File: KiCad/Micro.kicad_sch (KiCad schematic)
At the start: 0 parts

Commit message: Afegit el micro i les etapes del bus CAN i USART, també afegit el cristall i el debug
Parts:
- added C1, C2, C5, C6, C7, C8, C9: 100nF, symbol Device:C
- added C3, C4: 15pF, symbol Device:C
- added J1, J2: DE9_Pins, symbol Connector:DE9_Pins
- added J3: Conn_01x05, symbol Connector_Generic:Conn_01x05
- added R1: 120, symbol Device:R_US
- added U1: PIC24HJ128GP502, Package_SO:SOIC-28W_7.5x17.9mm_P1.27mm, symbol A_David_Puges_sym:PIC24HJ128GP502
- added U2: MCP2562-E-SN, Package_SO:SOIC-8_3.9x4.9mm_P1.27mm, symbol Interface_CAN_LIN:MCP2562-E-SN
- added U3: MAX3232, symbol Interface_UART:MAX3232
- added Y1: Crystal, Crystal:Crystal_HC49-U_Vertical, symbol Device:Crystal
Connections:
- new net: C5.1, U3.1 (C1+)
- new net: C5.2, U3.3 (C1-)
- new net: C7.1, U3.2 (VS+)
- new net: C4.1, U1.10 (RA6/OSC2_CLKOUT), Y1.1
- new net: U1.19 (VSS), U1.8 (VSS)
- new net: C3.1, U1.9 (RA7/OSC1_CLKIN), Y1.2
- new net: C8.1, U3.6 (VS-)
- new net: C6.1, U3.4 (C2+)
- new net: C6.2, U3.5 (C2-)
- new net CAN_ L: R1.2, U2.6 (CANL)
- new net CAN_H: J1.7, R1.1, U2.7 (CANH)
- new net CAN_L: J1.2
- new net CAN_RX: U1.24 (RB3), U2.4 (RXD)
- new net CAN_TX: U1.23 (RB2), U2.1 (TXD)
- new net GND: C1.2, C2.1, C3.2, C4.2, C7.2, C8.2, C9.2, J1.3, J3.3 (Pin_3), U2.2 (VSS), U2.8 (STBY), U3.15 (GND)
- new net PGC: J3.5 (Pin_5), U1.27 (RB6/PGC)
- new net PGD: J3.4 (Pin_4), U1.28 (RB7/PGD)
- new net R1_IN: J2.3, U3.13 (R1IN)
- new net Sortida_RL: C2.2, U2.5 (Vio)
- new net T1_OUT: J2.2, U3.14 (T1OUT)
- new net USART_RX: U1.18 (RC7), U3.12 (R1OUT)
- new net USART_TX: U1.17 (RC6), U3.11 (T1IN)
- new net sortida_RL: C1.1, C9.1, J3.2 (Pin_2), U1.20 (VDD), U2.3 (VDD), U3.16 (VCC)
- new net /MCLR: J3.1 (Pin_1), U1.1 (~{MCLR}/VPP/RE3)
- no-connect marks 0 -> 17

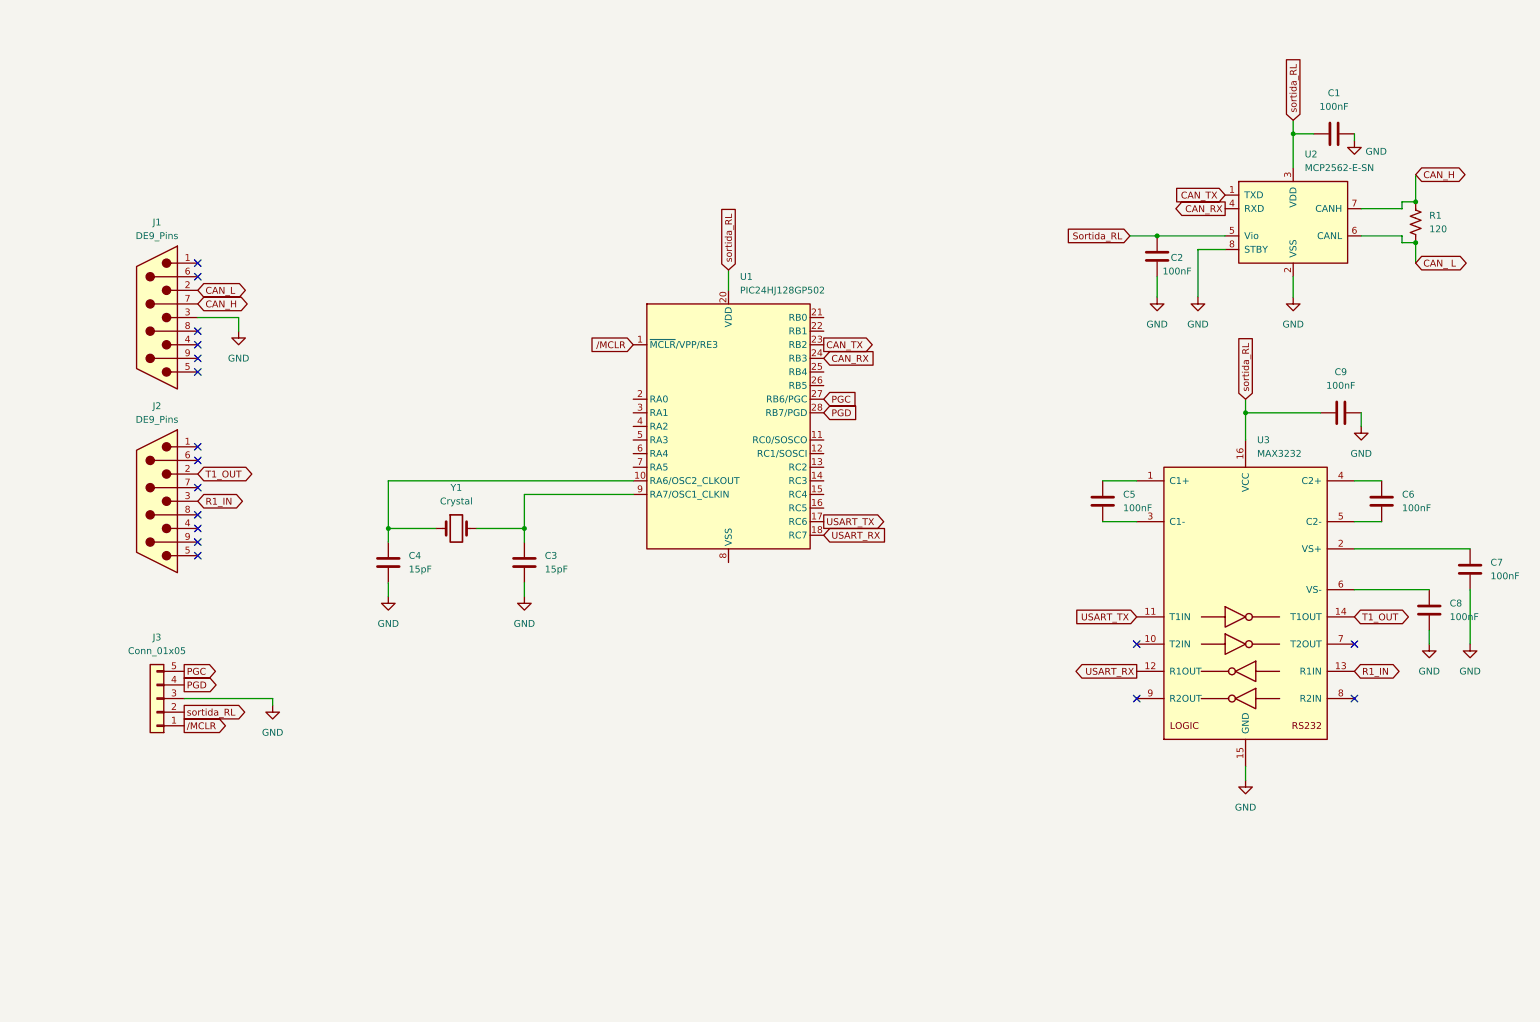
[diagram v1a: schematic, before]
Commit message: Feta la part digital del micro
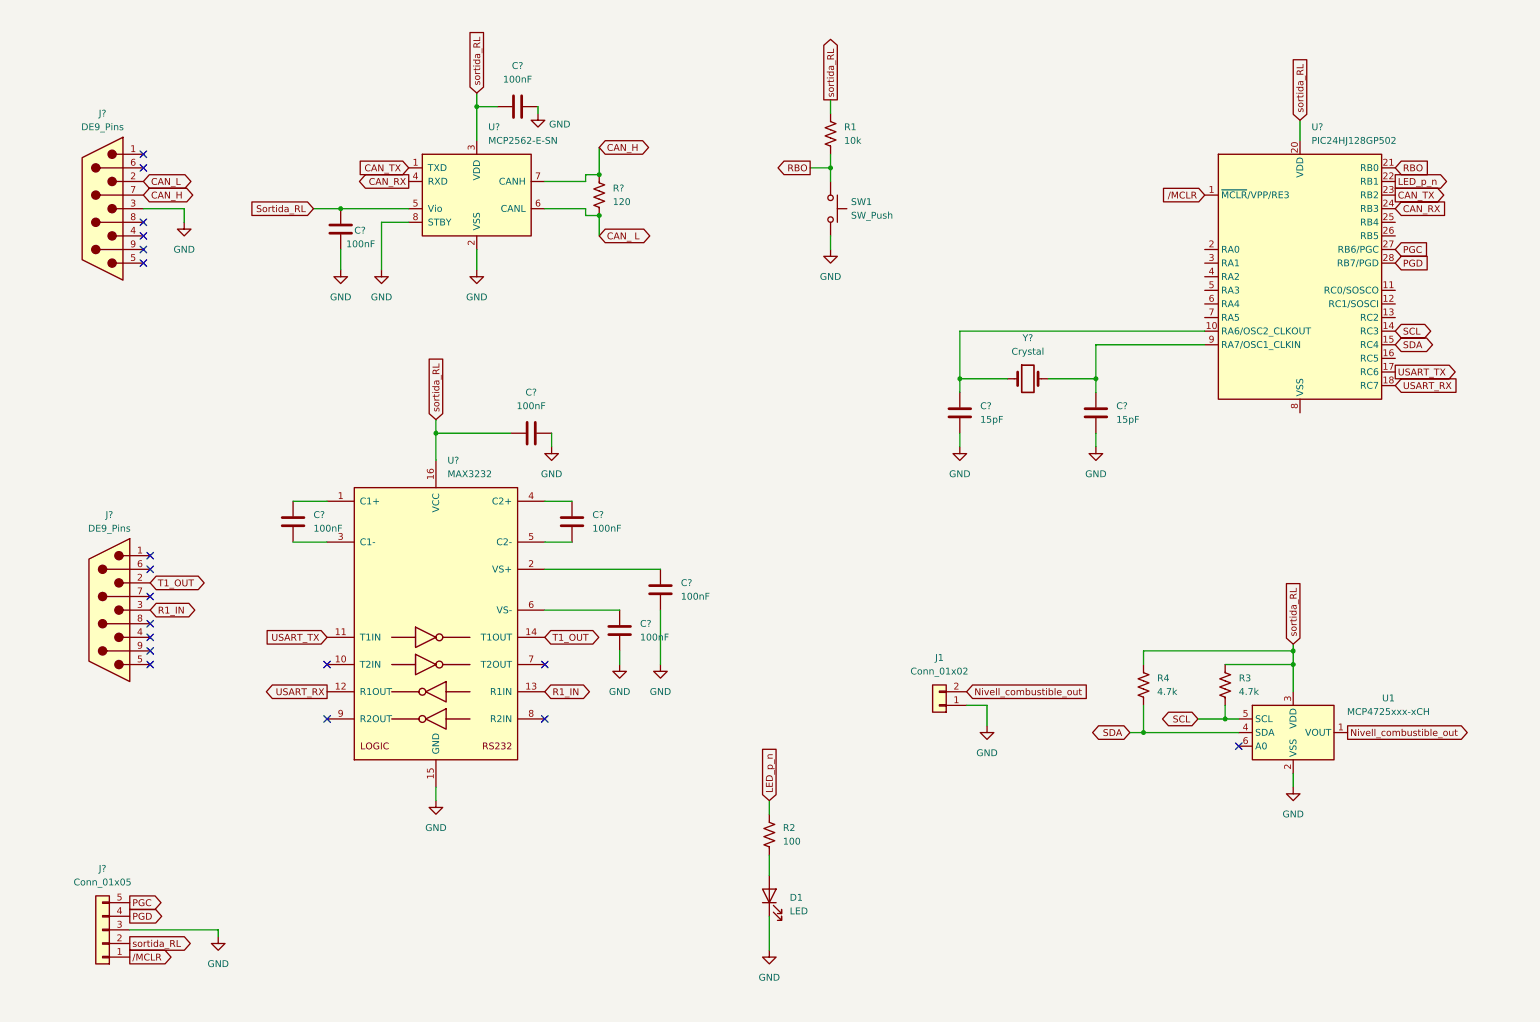
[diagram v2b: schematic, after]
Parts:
- added D1: LED, symbol Device:LED
- added J1: Conn_01x02, symbol Connector_Generic:Conn_01x02
- added R1: 10k, symbol Device:R_US
- added R2: 100, symbol Device:R_US
- added R3, R4: 4.7k, symbol Device:R_US
- added SW1: SW_Push, symbol Switch:SW_Push
- added U1: MCP4725xxx-xCH, Package_TO_SOT_SMD:SOT-23-6, symbol Analog_DAC:MCP4725xxx-xCH
- renumbered C5 to C?, C1 to C?, C7 to C?, C8 to C?, C9 to C?, C2 to C?, C6 to C?, C4 to C?, C3 to C?, J1 to J?, J2 to J?, J3 to J?, R1 to R?, U1 to U?, U2 to U?, U3 to U?, Y1 to Y?
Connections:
- net GND: now also D1.1 (K), J1.1 (Pin_1), SW1.2, U1.2 (VSS)
- net sortida_RL: now also R1.1, R3.1, R4.1, U1.3 (VDD)
- net SCL: now reaches U?.14 (RC3)
- net SCL: now also R3.2, U1.5 (SCL)
- net SDA: now reaches U?.15 (RC4)
- net SDA: now also R4.2, U1.4 (SDA)
- net RBO: now reaches U?.21 (RB0)
- net RBO: now also R1.2, SW1.1
- net LED_p_n: now reaches U?.22 (RB1)
- net LED_p_n: now also R2.1
- new net: D1.2 (A), R2.2
- new net Nivell_combustible_out: J1.2 (Pin_2), U1.1 (VOUT)
- no-connect marks 17 -> 18
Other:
- moved on the sheet: C?, J?, R?, U?, Y?

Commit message: millora etapa micro
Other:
- note added: "BLOC DE CONVERSIÓ DE COMBUSTIBLE (DAC)"
- note added: "BUS DE DADES CAN"
- note added: "I/O USUARI"
- note added: "Micro: PIC18F258 - Vdd = 3.3 V - Idd = 250 mA"
- note added: "Pulsador LED blau Resistència pull-up (10kohms) Resistència limitadora (100 ohms)"
- note added: "Transciever MCP2562 - Vdd = 3.3 V - Vio = 3.3V - Idd = 70 mA Resistència terminació 120 ohms (evita que rebotin els senyals elèctrics) Condensador desacoplament a Vdd"
- note added: "UNITAT CENTRAL DE PROCESSAMENT (MCU)"
- moved on the sheet: C?, D1, J1, J?, R1, R2, R3, R4, SW1, U1, U?, Y?

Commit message: millora micro
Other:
- note added: "MCP4725 - Vdd = 3.3 V - Idd = 400 micro A"
- note added: "SIMULADOR DE NIVELL ANALÒGIC"
- note removed: "BLOC DE CONVERSIÓ DE COMBUSTIBLE (DAC)"
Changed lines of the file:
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@@
+		)
+	)
+	(text "MCP4725\n - Vdd = 3.3 V\n        - Idd = 400 micro A"
+		(exclude_from_sim no)
+		(at 202.946 117.856 0)
+		(effects
+			(font
+				(size 1.27 1.27)
+				(thickness 0.254)
+				(bold yes)
+			)
 		)
 	)
@@
 		)
 	)
-	(text "BLOC DE CONVERSIÓ DE COMBUSTIBLE (DAC)"
+	(text "SIMULADOR DE NIVELL ANALÒGIC"
 		(exclude_from_sim no)
 		(at 219.964 110.744 0)
